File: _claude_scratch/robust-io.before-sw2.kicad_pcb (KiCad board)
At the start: 4 copper layers, 160 x 100 mm, 304 parts, among them J1 AVR-ISP-6, J10 Screw_Terminal_01x06, J14 Screw_Terminal_01x04, J15 Screw_Terminal_01x04, J16 Screw_Terminal_01x06, J18 Screw_Terminal_01x06, J19 Screw_Terminal_01x06, J20 UART, J3 Screw_Terminal_01x06, J4 Screw_Terminal_01x04, J5 Screw_Terminal_01x06, J6 Screw_Terminal_01x06, J9 Screw_Terminal_01x06, Q3 2N7002, Q4 2N7002, SW1 CHS-01TB, SW2 B3U-1000P, U1 DRV8876, U10 BTS7008, U11 BTS7008, U14 DRV8876, U2 ATmega1284P-A, U3 MCP2515, U4 TPS5604, U5 TPS5604, U6 MCP2562-E-MF, U7 MC33978, U8 BTS7008, U9 BTS7008, Y1 16MHz, Y2 12MHz

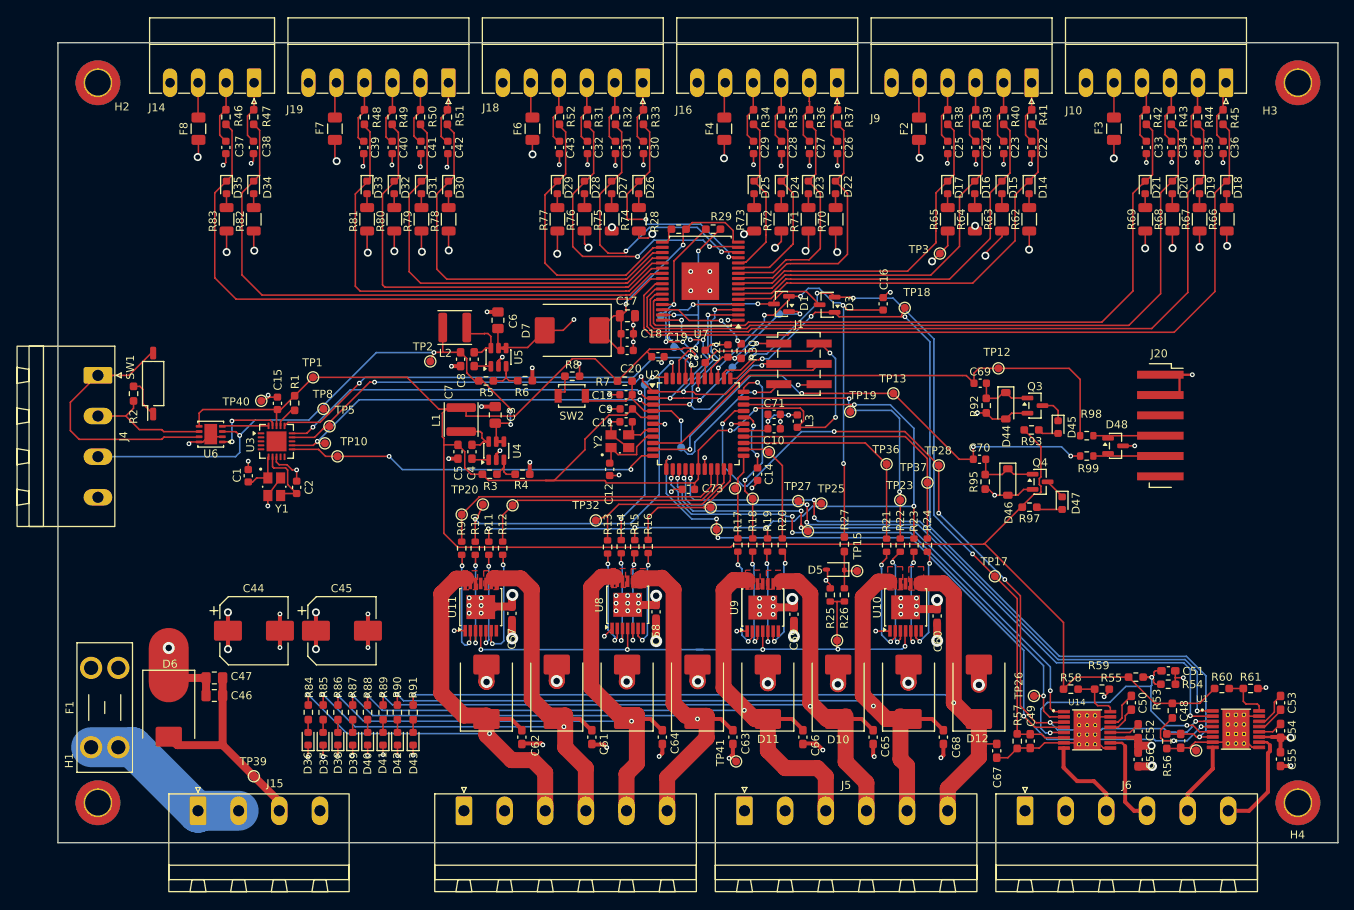
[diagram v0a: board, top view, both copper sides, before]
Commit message: Rev A: release to fab (JLCPCB, 5 PCB / 2 assembled)
Board
- Outline set to exactly 160 x 100 mm; plane zones resized to match
- UART brought out on J20 (1x6 SMD, FTDI pinout) with series
  resistors R98/R99 and TVS D48
- J1 and J20 changed to SMD headers (C52016780, C41417363)
- L1/L2 moved to Sunlord SWPA4030S footprints; regulator tracks rerouted
- 41 test points added (35 top, 6 bottom), including SPI access
- Crystal case pins (Y1/Y2 pads 2, 4) tied to GND
- SW2 changed to 2-pin push button symbol
- R84-R91 changed from 2.2k to 10k to cut dissipation at 24 V
- Thermal vias in U1/U14 enlarged to 0.3 mm drill; 27 +24V vias added
  under U8-U11; solid plane connections on high-current pins
- Input/output rows and edge connectors aligned
- /inputs/_SG4 track and via moved clear of R74 pad 1

Schematic
- ERC cleared: no-connects, PWR_FLAGs, pin types, off-grid items
- Symbols moved to project library robust-io
- Test point symbols added on processor and power sheets

Rules
- Custom DRC rule for U7 pad-to-pad clearance (0.15 mm)
- Minimum through hole 0.2 mm; silk-to-edge check ignored

Fab outputs (fab/)
- make_gerbers.sh: Gerbers, drill and position export via kicad-cli
- JLC BOM with LCSC part numbers on all 50 SMD lines
- JLC placement file with per-part rotation offsets
  (cpl_rotation_offsets.json), verified in JLC placement preview
- Through-hole BOM and test point list

DRC: 4 library-mismatch warnings (J20, U1, U14, U7), 0 errors
ERC: clean
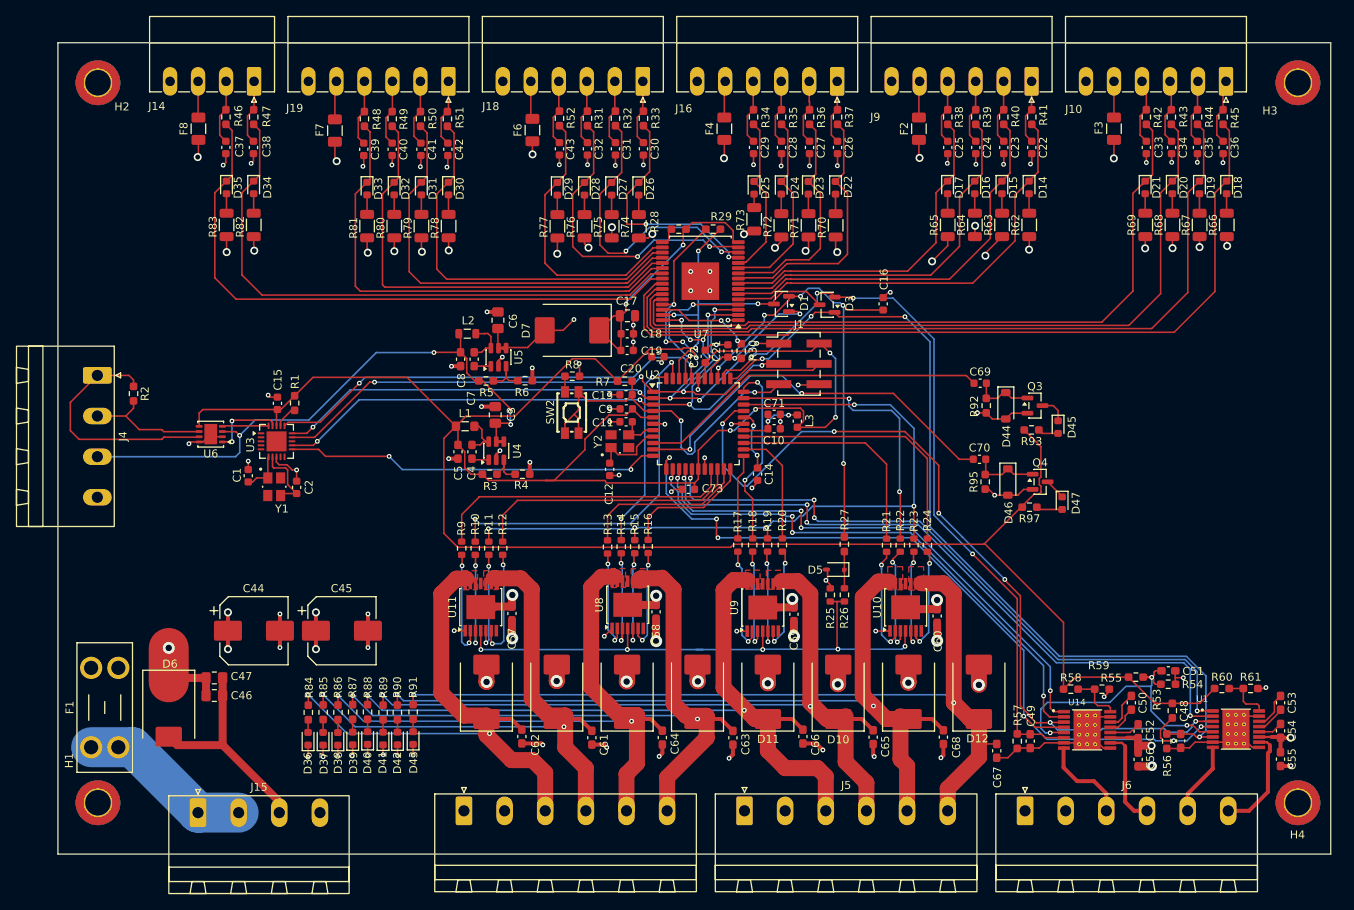
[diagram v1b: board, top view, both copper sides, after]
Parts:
- removed D48: SP0502BAHT, Package_TO_SOT_SMD:SOT-23
- removed J20: UART, Connector_PinHeader_2.54mm:PinHeader_1x06_P2.54mm_Vertical_SMD_Pin1Right
- removed R98, R99: 1k, Resistor_SMD:R_0603_1608Metric
- removed SW1: CHS-01TB, Button_Switch_SMD:SW_DIP_SPSTx01_Slide_Copal_CHS-01B_W7.62mm_P1.27mm
- removed TP1: +3.3V, TestPoint:TestPoint_Pad_D1.0mm
- removed TP10: INT_CAN0, TestPoint:TestPoint_Pad_D1.0mm
- removed TP11: RST, TestPoint:TestPoint_Pad_D1.0mm
- removed TP12: RX0, TestPoint:TestPoint_Pad_D1.0mm
- removed TP13: TX0, TestPoint:TestPoint_Pad_D1.0mm
- removed TP14: ISENSE, TestPoint:TestPoint_Pad_D1.0mm
- removed TP15: ISENSE_PROT, TestPoint:TestPoint_Pad_D1.0mm
- removed TP16: AMUX0, TestPoint:TestPoint_Pad_D1.0mm
- removed TP17: IPROPIM0, TestPoint:TestPoint_Pad_D1.0mm
- removed TP18: IPROPIM1, TestPoint:TestPoint_Pad_D1.0mm
- removed TP19: DSELn, TestPoint:TestPoint_Pad_D1.0mm
- removed TP2: +5V, TestPoint:TestPoint_Pad_D1.0mm
- removed TP20: DEN0, TestPoint:TestPoint_Pad_D1.0mm
- removed TP21: DEN1, TestPoint:TestPoint_Pad_D1.0mm
- removed TP22: DEN2, TestPoint:TestPoint_Pad_D1.0mm
- removed TP23: DEN3, TestPoint:TestPoint_Pad_D1.0mm
- removed TP24: EN_M0, TestPoint:TestPoint_Pad_D1.0mm
- removed TP25: EN_M1, TestPoint:TestPoint_Pad_D1.0mm
- removed TP26: PH_M0, TestPoint:TestPoint_Pad_D1.0mm
- removed TP27: PH_M1, TestPoint:TestPoint_Pad_D1.0mm
- removed TP28: nSLEEPMn, TestPoint:TestPoint_Pad_D1.0mm
- removed TP29: FAULTMn, TestPoint:TestPoint_Pad_D1.0mm
- removed TP3: +24V, TestPoint:TestPoint_Pad_D1.0mm
- removed TP30: DRV_OUT0, TestPoint:TestPoint_Pad_D1.0mm
- removed TP31: DRV_OUT1, TestPoint:TestPoint_Pad_D1.0mm
- removed TP32: DRV_OUT2, TestPoint:TestPoint_Pad_D1.0mm
- removed TP33: DRV_OUT3, TestPoint:TestPoint_Pad_D1.0mm
- removed TP34: DRV_OUT4, TestPoint:TestPoint_Pad_D1.0mm
- removed TP35: DRV_OUT5, TestPoint:TestPoint_Pad_D1.0mm
- removed TP36: DRV_OUT6, TestPoint:TestPoint_Pad_D1.0mm
- removed TP37: DRV_OUT7, TestPoint:TestPoint_Pad_D1.0mm
- removed TP38, TP39, TP40, TP41: GND, TestPoint:TestPoint_Pad_D1.0mm
- removed TP4: SCLK0, TestPoint:TestPoint_Pad_D1.0mm
- removed TP5: MOSI0, TestPoint:TestPoint_Pad_D1.0mm
- removed TP6: MISO0, TestPoint:TestPoint_Pad_D1.0mm
- removed TP7: CS_IN0, TestPoint:TestPoint_Pad_D1.0mm
- removed TP8: CS_CAN, TestPoint:TestPoint_Pad_D1.0mm
- removed TP9: INT_B0, TestPoint:TestPoint_Pad_D1.0mm
- L1: footprint Inductor_SMD:L_Sunlord_SWPA4030S -> Inductor_SMD:L_0805_2012Metric_Pad1.05x1.20mm_HandSolder
- L2: footprint Inductor_SMD:L_Sunlord_SWPA4030S -> Inductor_SMD:L_0805_2012Metric
- R84, R85, R86, R87, R88, R89, R90, R91: value 10k -> 2.2k
- SW2: value B3U-1000P -> EVQ-P9W02W; footprint Button_Switch_SMD:SW_SPST_B3U-1000P -> rml:KEY-SMD_EVQP9W02W
- moved SW2 2.08 mm to (94.2, 76.2)
- moved L2 1.75 mm to (81.2, 66.4)
- moved L1 0.98 mm to (80.9, 77.9), turned to 180 degrees
- moved R74 0.87 mm to (102.6, 52.9)
- moved R75 0.87 mm to (99.2, 52.9)
- moved R76 0.87 mm to (95.8, 52.9)
- moved R77 0.87 mm to (92.4, 52.9)
- moved R78 0.85 mm to (78.8, 52.9)
- moved R79 0.85 mm to (75.4, 52.9)
- moved R80 0.85 mm to (72.0, 52.9)
- moved R81 0.85 mm to (68.6, 52.9)
- moved R70 0.75 mm to (127.2, 52.8)
- moved R71 0.75 mm to (123.8, 52.8)
- moved R72 0.75 mm to (120.4, 52.8)
- moved R62 0.70 mm to (151.4, 52.8)
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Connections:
- R2 pad 1: Net-(R2-Pad1) -> Net-(J4-Pin_1)
- SW2 pad 2: Net-(SW2-D) -> /processor/RST
- Y1 pad 2: GND -> unconnected-(Y1-Pad2)
- Y1 pad 4: GND -> unconnected-(Y1-Pad4)
- Y2 pad 2: GND -> unconnected-(Y2-Pad2)
- Y2 pad 4: GND -> unconnected-(Y2-Pad4)
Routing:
- net /processor/RX0: track 66.4 -> 44.0 mm
- net GND: track 258.0 -> 239.5 mm, vias 103 -> 100
- net /processor/TX0: track 64.5 -> 49.2 mm, vias 4 -> 2
- net +24V: track 131.6 -> 118.2 mm, vias 67 -> 40
- net /processor/RST: track 36.3 -> 45.6 mm
- net /processor/TX0_EXT: track 7.89 -> 0.00 mm
- net /processor/RX0_EXT: track 7.89 -> 0.00 mm
- net Net-(R2-Pad1): track 4.94 -> 0.00 mm
- net Net-(J4-Pin_1): track 33.1 -> 30.5 mm
- net DEN0: track 49.3 -> 46.8 mm
- net DRV_OUT2: track 22.6 -> 21.0 mm
- net ISENSE_PROT: track 6.85 -> 5.25 mm
- net +3.3V: track 366.9 -> 368.4 mm
- net EN_M0: track 68.4 -> 67.2 mm
- net IPROPIM1: track 110.4 -> 109.2 mm
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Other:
- board size 160 x 100 mm -> 159.1 x 101.4 mm
